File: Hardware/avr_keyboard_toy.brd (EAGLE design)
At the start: 40.3 x 80 mm, 20 parts, among them IC1 7805T, IC2 MCP23017SP, U1 ATMEGA328P-PU

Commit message: Routing signals progress
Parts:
- moved S1 0.90 mm to (21.6, 6.35)
- moved SP1 0.63 mm to (11.4, 6.35)
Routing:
- net +3V3: track 0.00 -> 141.2 mm, vias 0 -> 4
- net VCC: track 7.62 -> 132.1 mm, vias 0 -> 2
- net +5V: track 0.00 -> 101.1 mm
- net DSP_A0: track 0.00 -> 52.1 mm, vias 0 -> 2
- net TFT_EN: track 0.00 -> 41.9 mm
- net SD_SS: track 0.00 -> 40.6 mm, vias 0 -> 3
- net SCK: track 5.08 -> 43.2 mm, vias 0 -> 1
- net RST: track 37.4 -> 73.2 mm, vias 1 -> 0
- net MOSI: track 12.7 -> 46.4 mm, vias 0 -> 2
- net PIEZO: track 0.00 -> 31.1 mm
- net SD_EN: track 0.00 -> 30.5 mm, vias 0 -> 2
- net MISO: track 10.2 -> 32.3 mm
- net DSP_RST: track 48.8 -> 55.1 mm
- net N$4: track 0.00 -> 4.48 mm
- net SS: track 36.3 -> 33.7 mm, vias 0 -> 2

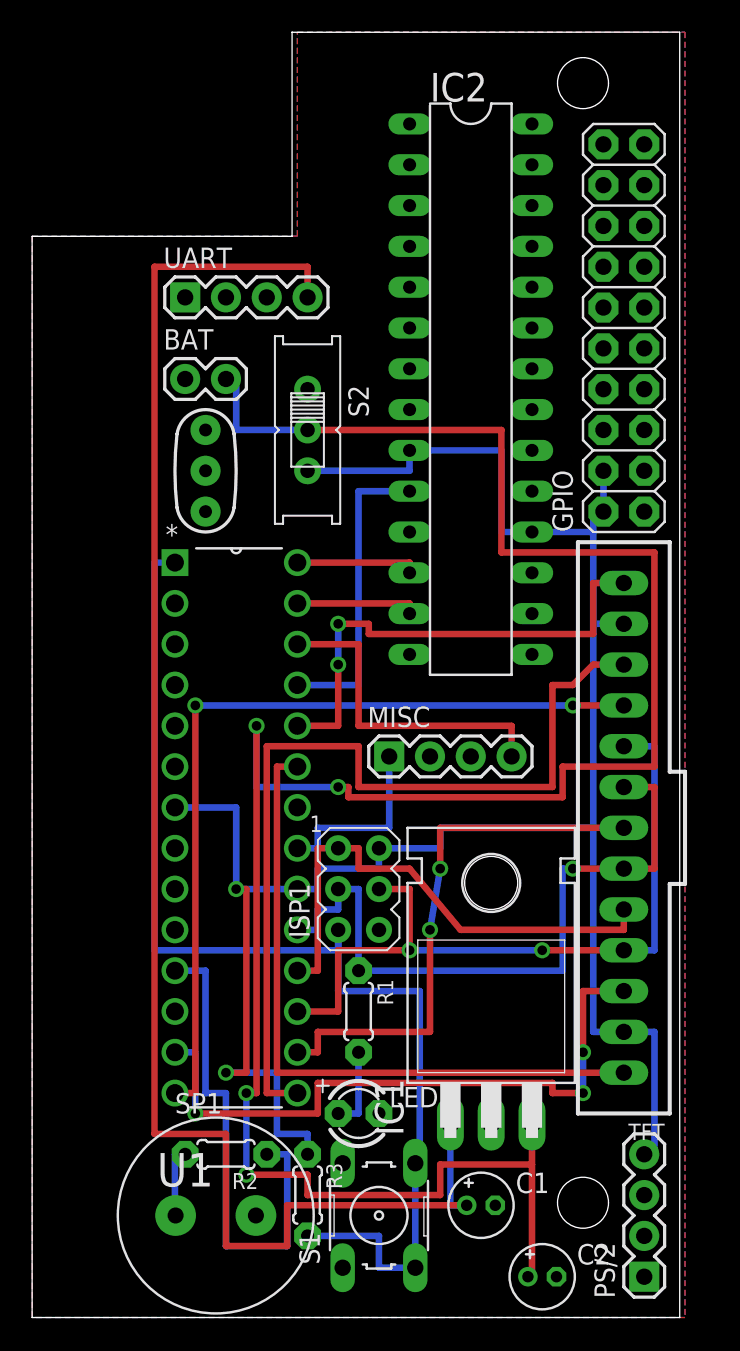
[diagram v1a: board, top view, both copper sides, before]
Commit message: Finished routing signals
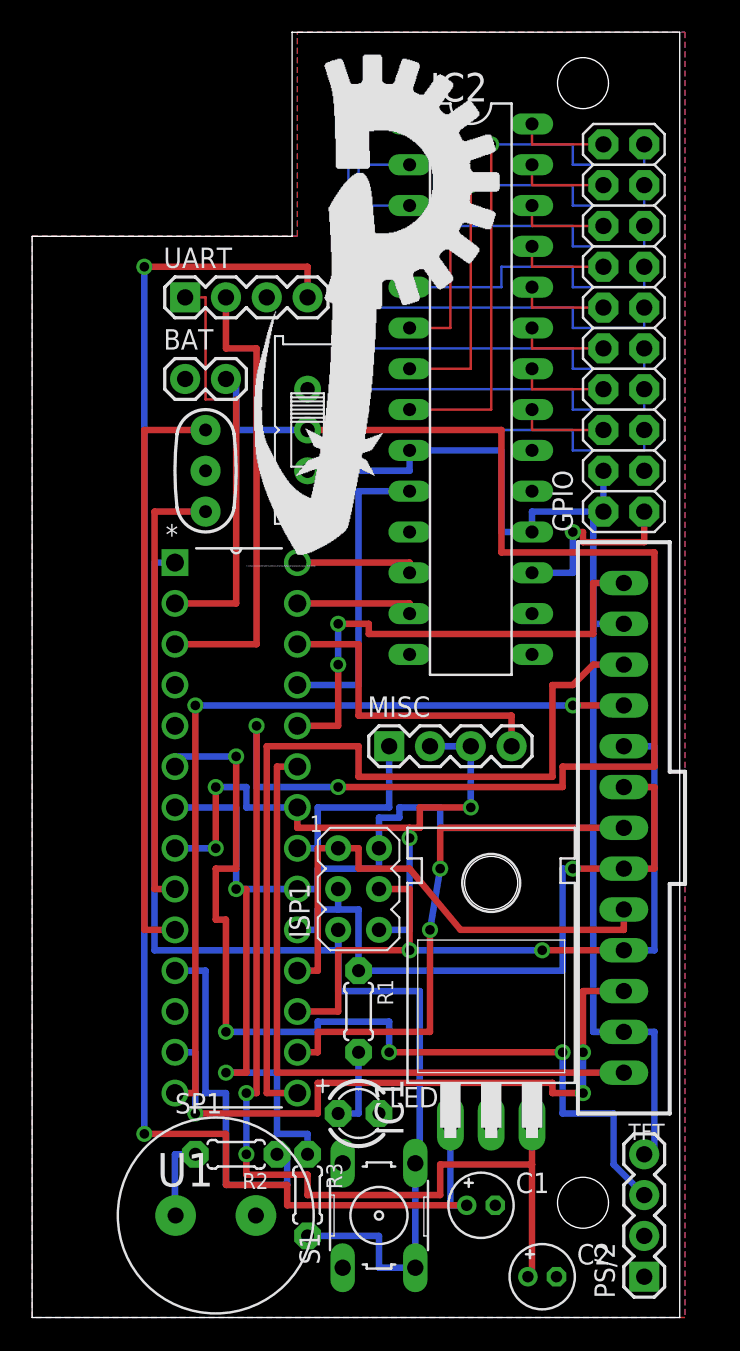
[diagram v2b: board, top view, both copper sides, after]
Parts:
- added U$1, U$2: (no value), petezah:LOGO_SM
- moved MISC 0.64 mm to (22.2, 35.6)
- moved R2 0.63 mm to (12.7, 10.2)
- turned XTAL1 to 90 degrees
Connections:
- net GND: now also MISC.2, MISC.3
- net PD2: no longer MISC.2
- net PD6: no longer MISC.3
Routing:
- net PS/2_DATA: track 0.00 -> 59.8 mm, vias 0 -> 4
- net GND: track 0.00 -> 52.7 mm, vias 0 -> 5
- net GPB0: track 0.00 -> 43.8 mm
- net GPB1: track 0.00 -> 37.5 mm
- net N$2: track 0.00 -> 36.8 mm
- net GPB7: track 0.00 -> 33.7 mm, vias 0 -> 1
- net GPB2: track 0.00 -> 31.1 mm
- net TX: track 0.00 -> 28.6 mm
- net GPB6: track 0.00 -> 28.6 mm, vias 0 -> 1
- net N$1: track 0.00 -> 27.9 mm
- net RX: track 0.00 -> 26.0 mm
- net GPB3: track 0.00 -> 24.8 mm
- net GPB5: track 0.00 -> 23.5 mm, vias 0 -> 1
- net GPB4: track 0.00 -> 18.4 mm
- net PIEZO: track 31.1 -> 22.9 mm
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
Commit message: Finished layout for rev. A board
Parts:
- added D2, D6: TPB1,27, testpad:B1,27
- R1: value (none) -> 120
- R2: value (none) -> 560
- R3: value (none) -> 10k
- U$1: device petezah:LOGO_SM -> petezah:LOGO_TINY
- moved U$1 23.3 mm to (17.8, 69.8)
- moved U$2 6.02 mm to (32.4, 38.1)
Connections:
- removed net PS/2_CLK: U1.5
- net PD2: now also D2.TP
- net PD6: now also D6.TP
- net PS/2_CLOCK: now also U1.5
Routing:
- net PS/2_CLOCK: track 0.00 -> 123.6 mm, vias 0 -> 6
- net PD2: track 0.00 -> 2.54 mm
- net PD6: track 0.00 -> 1.91 mm
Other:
- board size 40.3 x 80 mm -> 37.1 x 80 mm
- board text added: "(c) 2016 Peter Dunshee @Petezah petezah.com"
- board text added: "+"
- board text added: "+3V3"
- board text added: "+5V"
- board text added: "0"
- board text added: "1"
- board text added: "10k"
- board text added: "120"
- board text added: "2"
- board text added: "3"
- board text added: "4"
- board text added: "5"
- board text added: "560"
- board text added: "6"
- board text added: "7"
- board text added: "A"
- board text added: "AREF"
- board text added: "AVR Keyboard Toy Board revision A"
- board text added: "B"
- board text added: "C3"
- board text added: "CLOCK"
- board text added: "DATA"
- board text added: "DSP_A0"
- board text added: "DSP_MOSI"
- board text added: "DSP_RST"
- board text added: "DSP_SCK"
- board text added: "DSP_SS"
- board text added: "DSP_VCC"
- board text added: "G"
- board text added: "GND"
- board text added: "MISO VCC SCK MOSI RST GND"
- board text added: "Petezah"
- board text added: "RX"
- board text added: "SD_EN"
- board text added: "SD_MISO"
- board text added: "SD_MOSI"
- board text added: "SD_SCK"
- board text added: "SD_SS"
- board text added: "TFT_EN"
- board text added: "TFT_VCC"
- board text added: "TX"

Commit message: Working on Rev B of hardware
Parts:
- removed C1, C2: 10uF, adafruit:E1,8-4
- removed IC1: 7805T, adafruit:TO220H
- IC2: value MCP23017SP -> MCP23017SO; device adafruit:DIL28-3 -> adafruit:SO28W
- U1: value ATMEGA328P-PU -> ATMEGA328P-AU; device Atmel_By_element14_Batch_1-00:DIP254P762X457-28 -> Atmel_By_element14_Batch_1-00:QFP80P900X900X120-32N
- moved U1 15.3 mm to (12.1, 28.6)
- moved IC2 4.49 mm to (26.7, 62.2)
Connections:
- new net ADC6: U1.19
- new net ADC7: U1.22
- net +3V3: no longer C2.+, IC1.3
- net +5V: no longer C1.+, IC1.1
- net AREF: now also U1.20; no longer U1.21
- net DSP_A0: now also U1.12; no longer U1.14
- net DSP_RST: now also U1.13; no longer U1.15
- net GND: now also U1.21, U1.3, U1.5; no longer C1.-, C2.-, IC1.2, U1.22, U1.8
- net MISO: now also U1.16; no longer U1.18
- net MOSI: now also U1.15; no longer U1.17
- net N$1: now also U1.7; no longer U1.9
- net N$2: now also U1.8; no longer U1.10
- net PD2: now also U1.32; no longer U1.4
- net PD6: now also U1.10; no longer U1.12
- net PIEZO: now also U1.9; no longer U1.11
- net PS/2_CLOCK: now also U1.1; no longer U1.5
- net PS/2_DATA: now also U1.2; no longer U1.6
- net RST: now also U1.29; no longer U1.1
- net RX: now also U1.30; no longer U1.2
- net SCK: now also U1.17; no longer U1.19
- net SD_SS: now also U1.11; no longer U1.13
- net SS: now also U1.14; no longer U1.16
- net TX: now also U1.31; no longer U1.3
- net VCC: now also U1.18, U1.4, U1.6; no longer U1.20, U1.7
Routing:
- net +3V3: track 140.0 -> 0.00 mm, vias 4 -> 0
- net VCC: track 135.9 -> 0.00 mm, vias 2 -> 0
- net PS/2_CLOCK: track 123.6 -> 0.00 mm, vias 6 -> 0
- net +5V: track 97.3 -> 0.00 mm, vias 2 -> 0
- net RST: track 73.2 -> 0.00 mm
- net PS/2_DATA: track 59.8 -> 0.00 mm, vias 4 -> 0
- net DSP_RST: track 53.9 -> 0.00 mm
- net GND: track 52.7 -> 0.00 mm, vias 5 -> 0
- net DSP_A0: track 52.1 -> 0.00 mm, vias 2 -> 0
- net MOSI: track 46.4 -> 0.00 mm, vias 2 -> 0
- net GPB0: track 43.8 -> 0.00 mm
- net TFT_EN: track 41.9 -> 0.00 mm
- net SCK: track 41.9 -> 0.00 mm, vias 1 -> 0
- net SD_SS: track 40.6 -> 0.00 mm, vias 3 -> 0
- net GPB1: track 37.5 -> 0.00 mm
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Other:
- board text added: "AVR Keyboard Toy Board revision B"
- board text removed: "AVR Keyboard Toy Board revision A"

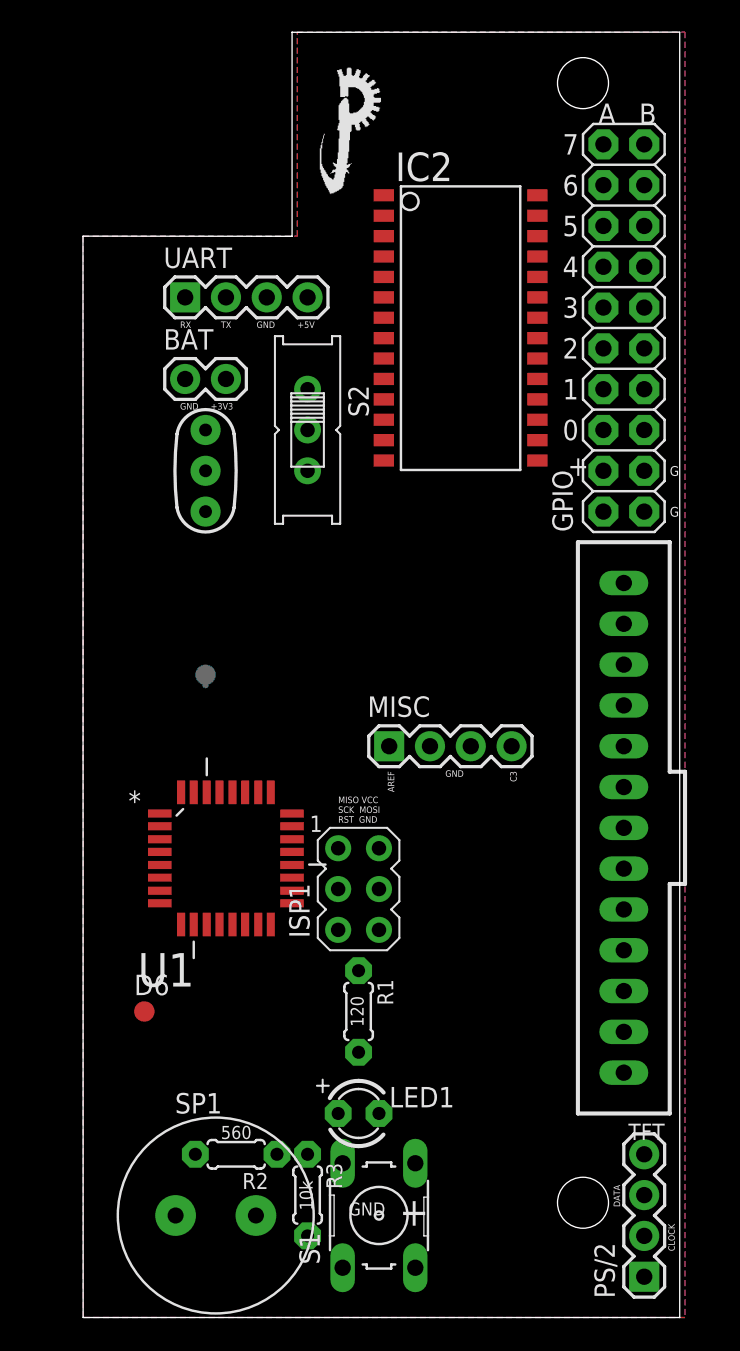
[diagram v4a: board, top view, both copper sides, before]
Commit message: Added SID test, and made rev B of board
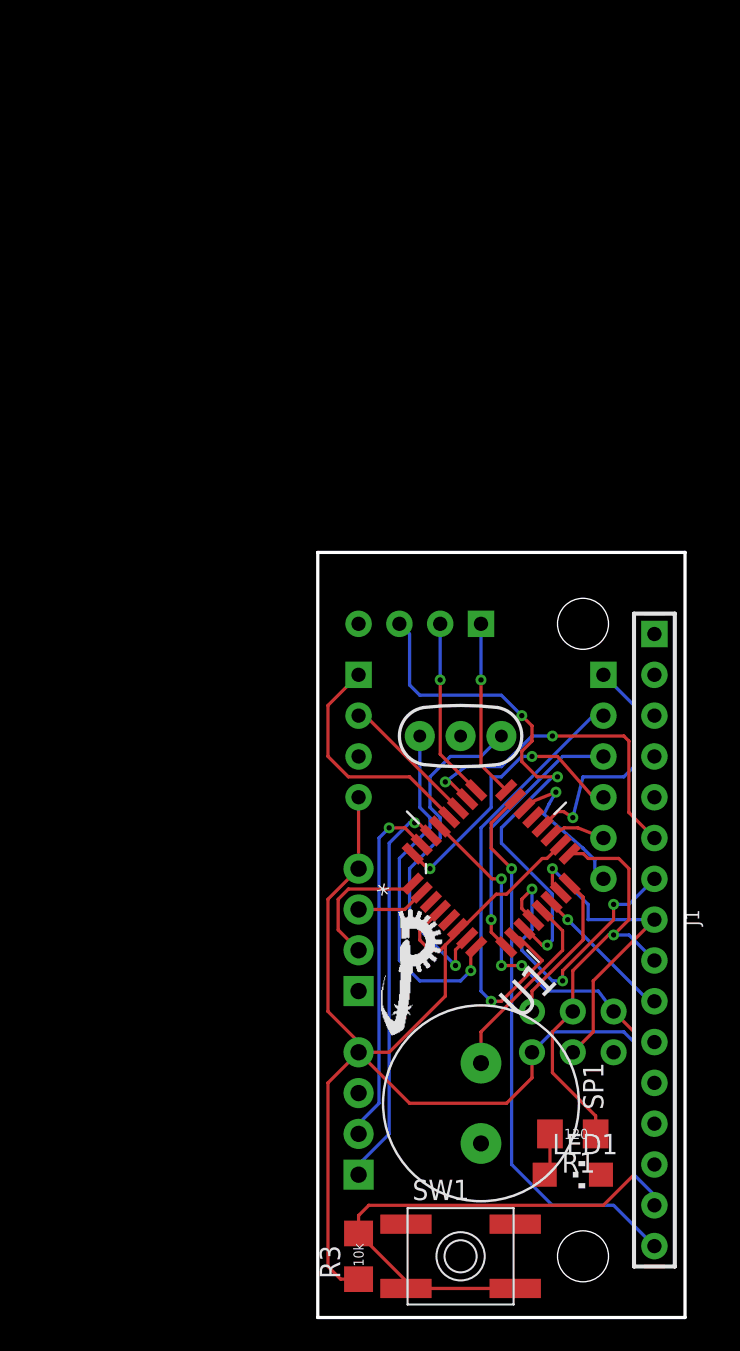
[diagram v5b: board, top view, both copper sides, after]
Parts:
- removed BAT: (no value), SparkFun-Connectors:1X02
- removed D2, D6: TPB1,27, testpad:B1,27
- removed GPIO: (no value), SparkFun-Connectors:2X10
- removed IC2: MCP23017SO, adafruit:SO28W
- removed MISC: (no value), SparkFun-Connectors:1X04
- removed R2: 560, adafruit:0204/5
- removed S1: (no value), switch-omron:B3F-10XX
- removed S2: (no value), adafruit:EG1218
- removed TFT: C-GRID-13-70543, con-molex:70543-13
- added CN1: MISC, Seeed-Connector -2016:H6-2.54
- added J1: TFT, Seeed-OPL-Connector:H16-2.54
- added J2: I2C, Seeed-Connector -2016:H4-2.54
- added J3: MISC2, Seeed-Connector -2016:H4-2.54
- added SW1: SPST_TACT-EVQQ2, adafruit:EVQ-Q2
- LED1: device adafruit:LED3MM -> adafruit:CHIPLED_1206
- R1, R3: device adafruit:0204/5 -> adafruit:R1206
- moved UART 55.7 mm to (20.3, 8.89), flipped to the bottom, turned to 90 degrees
- moved U$1 52.5 mm to (21.6, 17.5)
- moved PS/2 25.1 mm to (20.3, 20.3), flipped to the bottom
- moved XTAL1 22.9 mm to (26.7, 36.2), turned to 180 degrees
- moved U$2 19.7 mm to (31.1, 18.4)
- moved SP1 17.9 mm to (27.9, 13.3), turned to 270 degrees
- moved U1 16.5 mm to (28.6, 27.9), turned to 45 degrees
- moved ISP1 16.0 mm to (33.7, 17.8), flipped to the bottom, turned to 270 degrees
- moved R1 15.4 mm to (33.7, 11.4), turned to 180 degrees
- moved LED1 13.9 mm to (33.7, 8.89), turned to 270 degrees
- moved R3 4.96 mm to (20.3, 3.81), turned to 90 degrees
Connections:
- removed net +3V3: BAT.2, S2.P
- removed net +5V: UART.4
- removed net GPA0: GPIO.6, IC2.21
- removed net GPA1: GPIO.8, IC2.22
- removed net GPA2: GPIO.10, IC2.23
- removed net GPA3: GPIO.12, IC2.24
- removed net GPA4: GPIO.14, IC2.25
- removed net GPA5: GPIO.16, IC2.26
- removed net GPA6: GPIO.18, IC2.27
- removed net GPA7: GPIO.20, IC2.28
- removed net GPB0: GPIO.5, IC2.1
- removed net GPB1: GPIO.7, IC2.2
- removed net GPB2: GPIO.9, IC2.3
- removed net GPB3: GPIO.11, IC2.4
- removed net GPB4: GPIO.13, IC2.5
- removed net GPB5: GPIO.15, IC2.6
- removed net GPB6: GPIO.17, IC2.7
- removed net GPB7: GPIO.19, IC2.8
- removed net MCP_EN: IC2.10, U1.25
- removed net N$4: R2.2, SP1.P$1
- removed net PC3: MISC.4, U1.26
- removed net SD_EN: TFT.13, U1.24
- removed net SD_SS: TFT.3, U1.11
- new net PC1: J3.1, U1.24
- new net PC2: J3.2, U1.25
- new net PD5: CN1.3, U1.9
- new net PD7: J3.3, U1.11
- net ADC6: now also CN1.5
- net ADC7: now also CN1.6
- net AREF: now also CN1.1; no longer MISC.1
- net DSP_A0: now also J1.7; no longer TFT.10
- net DSP_RST: now also J1.6, U1.26; no longer TFT.11, U1.13
- net GND: now also J2.3, J3.4, LED1.C, SW1.B, SW1.B'; no longer BAT.1, GPIO.1, GPIO.3, IC2.15, IC2.16, IC2.17, LED1.K, MISC.2, MISC.3, S1.1, S1.2
- net MISO: no longer TFT.5
- net MOSI: now also J1.8; no longer TFT.4, TFT.9
- net PD2: now also CN1.4; no longer D2.TP
- net PD6: now also CN1.2; no longer D6.TP
- net PIEZO: now also SP1.P$1, U1.13; no longer R2.1, U1.9
- net RST: now also SW1.A, SW1.A'; no longer S1.3, S1.4
- net SCK: now also J1.9; no longer TFT.6, TFT.8
- net SCL: now also J2.1; no longer IC2.12
- net SDA: now also J2.2; no longer IC2.13
- net SS: now also J1.10; no longer TFT.7
- net TFT_EN: now also J1.16; no longer TFT.1
- net VCC: now also J1.15, J2.4, UART.4; no longer GPIO.2, GPIO.4, IC2.18, IC2.9, S2.S, TFT.12, TFT.2
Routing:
- net VCC: track 0.00 -> 90.2 mm
- net RST: track 0.00 -> 60.3 mm, vias 0 -> 3
- net TFT_EN: track 0.00 -> 34.9 mm, vias 0 -> 1
- net PD7: track 0.00 -> 33.2 mm, vias 0 -> 3
- net PD6: track 0.00 -> 28.1 mm, vias 0 -> 1
- net SCK: track 0.00 -> 27.1 mm, vias 0 -> 1
- net RX: track 0.00 -> 24.9 mm, vias 0 -> 1
- net TX: track 0.00 -> 22.3 mm, vias 0 -> 1
- net N$2: track 0.00 -> 21.9 mm, vias 0 -> 1
- net N$1: track 0.00 -> 21.5 mm, vias 0 -> 1
- net DSP_RST: track 0.00 -> 21.2 mm, vias 0 -> 2
- net MOSI: track 0.00 -> 20.3 mm, vias 0 -> 1
- net DSP_A0: track 0.00 -> 19.2 mm, vias 0 -> 3
- net PD2: track 0.64 -> 17.4 mm, vias 0 -> 2
- net PD5: track 0.00 -> 16.6 mm, vias 0 -> 1
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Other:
- board size 37.1 x 80 mm -> 22.9 x 47.6 mm
- board text added: "ADC6"
- board text added: "ADC7"
- board text added: "GND RST MOSI SCK VCC MISO"
- board text added: "PC1"
- board text added: "PC2"
- board text added: "PD2"
- board text added: "PD5"
- board text added: "PD6"
- board text added: "PD7"
- board text added: "SCL"
- board text added: "SDA"
- board text added: "VCC"
- board text removed: "+"
- board text removed: "+3V3"
- board text removed: "+5V"
- board text removed: "0"
- board text removed: "1"
- board text removed: "2"
- board text removed: "3"
- board text removed: "4"
- board text removed: "5"
- board text removed: "560"
- board text removed: "6"
- board text removed: "7"
- board text removed: "A"
- board text removed: "B"
- board text removed: "C3"
- board text removed: "DSP_VCC"
- board text removed: "G"
- board text removed: "MISO VCC SCK MOSI RST GND"
- board text removed: "SD_EN"
- board text removed: "SD_MISO"
- board text removed: "SD_MOSI"
- board text removed: "SD_SCK"
- board text removed: "SD_SS"
